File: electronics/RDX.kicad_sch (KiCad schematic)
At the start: 47 parts, among them SW1 Rotary Encoder Module, U1 PCA9685PW

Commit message: revision 1.1.0 of electronics
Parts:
- CTRL.U2: renamed from U1; value PCA9685PW -> PCA9685 - Servo board
- renumbered STEP.J5 to CTRL.J1, CTRL.J1 to CTRL.J2, CTRL.J2 to CTRL.J3, CTRL.J3 to CTRL.J4, PER.M1 to OUT.M1, SW1 to OUT.SW1, PSU.SW2 to OUT.SW2, PER.U1 to OUT.U1
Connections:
- net SDA: now reaches CTRL.J3., CTRL.U1.3 (IO2)
- net SCL: now reaches CTRL.J4., CTRL.U1.5 (IO3)
- new net: STEP.J2., STEP.U2. (B2) (x3)
- new net: STEP.J4., STEP.U4. (B2) (x3)
- new net: STEP.J1., STEP.U1. (B2) (x3)
- new net: STEP.J3., STEP.U3. (B2) (x3)
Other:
- note added: "CTRL.U1.14"
- note added: "PANEL I - Stepper Panel"
- note added: "PANEL II - Control panel"
- note added: "PANEL III - Power panel"
- moved on the sheet: OUT.M1, OUT.STEP1, OUT.STEP2, OUT.STEP3, OUT.STEP4, OUT.SV1, OUT.SV2, OUT.SV3, OUT.SV4, OUT.SV5, OUT.SV6, OUT.SW1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

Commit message: starting electronics and contruction syncronization
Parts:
- renumbered STEP.J1 to A2.J1_1, STEP.J2 to A2.J1_2, STEP.J3 to A2.J1_3, STEP.J4 to A2.J1_4, STEP.U1 to A2.U1_1, STEP.U2 to A2.U1_2, STEP.U3 to A2.U1_3, STEP.U4 to A2.U1_4, PSU.J01 to A4.J01, PSU.J02 to A4.J02, PSU.J11 to A4.J11, PSU.J12 to A4.J12, PSU.J21 to A4.J21, PSU.J22 to A4.J22, PSU.PS1 to A4.PS1, PSU.PS11 to A4.PS11, PSU.PS12 to A4.PS12, PSU.PS13 to A4.PS13
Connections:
- new net: A2.J1_2., A2.U1_2. (B2) (x3)
- new net: A2.J1_4., A2.U1_4. (B2) (x3)
- new net: A2.J1_1., A2.U1_1. (B2) (x3)
- new net: A2.J1_3., A2.U1_3. (B2) (x3)
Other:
- note added: "A2 - PANEL I - Stepper Panel"
- note added: "A3 - PANEL II - Control panel"
- note added: "A3.J2 (5V)"
- note added: "A4 - PANEL III - Power panel"
- note added: "A4.J12 (36V)"
- note added: "The controller includes 4 high performace stepper drivers that can be calibrated for microstepping manually See the table for pin mappings to the RPi GPIOs"
- note removed: "PANEL I - Stepper Panel"
- note removed: "PANEL II - Control panel"
- note removed: "PANEL III - Power panel"
- note removed: "STEP.J5 (5V)"
- note removed: "The controller includes 3 high performace stepper drivers that can be calibrated for microstepping manually See the table for pin mappings to the RPi GPIOs"
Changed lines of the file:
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@@
 		)
 	)
-	(text "PANEL III - Power panel"
+	(text "A4 - PANEL III - Power panel"
 		(exclude_from_sim no)
 		(at 20.32 276.606 0)
@@
 		)
 	)
-	(text "PANEL I - Stepper Panel"
+	(text "A2 - PANEL I - Stepper Panel"
 		(exclude_from_sim no)
 		(at 20.32 21.844 0)
@@
 		)
 	)
-	(text "PANEL II - Control panel"
+	(text "A3 - PANEL II - Control panel"
 		(exclude_from_sim no)
 		(at 299.72 22.352 0)
@@
 		)
 	)
-	(text "The controller includes 3 high performace stepper drivers\nthat can be calibrated for microstepping manually\n\nSee the table for pin mappings to the RPi GPIOs"
+	(text "The controller includes 4 high performace stepper drivers\nthat can be calibrated for microstepping manually\n\nSee the table for pin mappings to the RPi GPIOs"
 		(exclude_from_sim no)
 		(at 121.412 168.91 0)
@@
 		)
 	)
-	(text "PSU.J12 (36V)"
+	(text "A4.J12 (36V)"
 		(exclude_from_sim no)
 		(at 67.818 85.852 0)
@@
 		)
 	)
-	(text "STEP.J5 (5V)"
+	(text "A3.J2 (5V)"
 		(exclude_from_sim no)
 		(at 49.53 85.598 0)
@@
 		)
 	)
+	(polyline
+		(pts
+			(xy 19.05 220.98) (xy 54.61 220.98)
+		)
+		(stroke
+			(width 0)
+			(type dash)
+		)
+	)
 	(wire
 		(pts
@@
 		)
 	)
+	(polyline
+		(pts
+			(xy 54.61 186.69) (xy 54.61 191.77)
+		)
+		(stroke
+			(width 0)
+			(type dash)
+		)
+	)
 	(wire
 		(pts
@@
 		)
 	)
+	(polyline
+		(pts
+			(xy 54.61 201.93) (xy 54.61 220.98)
+		)
+		(stroke
+			(width 0)
+			(type dash)
+		)
+	)
 	(wire
 		(pts
@@
 		(on_board yes)
 		(dnp no)
-		(property "Reference" "PSU.J02"
+		(property "Reference" "A4.J02"
 			(at 99.06 239.776 0)
 			(effects
@@
 			(project "RDX"
 				(path "/ae012dcf-7a16-4b89-bb28-202da592e0ac"
-					(reference "PSU.J02")
+					(reference "A4.J02")
 					(unit 1)
 				)
@@
 		(on_board yes)
 		(dnp no)
-		(property "Reference" "STEP.J2"
+		(property "Reference" "A2.J1_2"
 			(at 106.172 69.85 90)
 			(effects
@@
 			(project "RDX"
 				(path "/ae012dcf-7a16-4b89-bb28-202da592e0ac"
-					(reference "STEP.J2")
+					(reference "A2.J1_2")
 					(unit 1)
 				)
@@
 		(on_board yes)
 		(dnp no)
-		(property "Reference" "STEP.U4"
+		(property "Reference" "A2.U1_4"
 			(at 137.668 109.982 0)
 			(effects
@@
 			(project "RDX"
 				(path "/ae012dcf-7a16-4b89-bb28-202da592e0ac"
-					(reference "STEP.U4")
+					(reference "A2.U1_4")
 					(unit 1)
 				)
@@
 		(on_board yes)
 		(dnp no)
-		(property "Reference" "STEP.J1"
+		(property "Reference" "A2.J1_1"
 			(at 37.592 69.85 90)
 			(effects
@@
 			(project ""
 				(path "/ae012dcf-7a16-4b89-bb28-202da592e0ac"
-					(reference "STEP.J1")
+					(reference "A2.J1_1")
 					(unit 1)
 				)
@@
 		(on_board yes)
 		(dnp no)
-		(property "Reference" "PSU.J22"
+		(property "Reference" "A4.J22"
 			(at 137.16 214.63 0)
 			(effects
@@
 			(project "RDX"
 				(path "/ae012dcf-7a16-4b89-bb28-202da592e0ac"
-					(reference "PSU.J22")
+					(reference "A4.J22")
 					(unit 1)
 				)
@@
 		(on_board yes)
 		(dnp no)
-		(property "Reference" "PSU.J01"
+		(property "Reference" "A4.J01"
 			(at 99.06 229.616 0)
 			(effects
@@
 			(project ""
 				(path "/ae012dcf-7a16-4b89-bb28-202da592e0ac"
-					(reference "PSU.J01")
+					(reference "A4.J01")
 					(unit 1)
 				)
@@
 		(on_board yes)
 		(dnp no)
-		(property "Reference" "STEP.J3"
+		(property "Reference" "A2.J1_3"
 			(at 37.592 142.24 90)
 			(effects
@@
 			(project "RDX"
 				(path "/ae012dcf-7a16-4b89-bb28-202da592e0ac"
-					(reference "STEP.J3")
+					(reference "A2.J1_3")
 					(unit 1)
 				)
@@
 		(dnp no)
 		(fields_autoplaced yes)
-		(property "Reference" "PSU.J21"
+		(property "Reference" "A4.J21"
 			(at 139.7 204.47 0)
 			(effects
@@
 			(project "RDX"
 				(path "/ae012dcf-7a16-4b89-bb28-202da592e0ac"
-					(reference "PSU.J21")
+					(reference "A4.J21")
 					(unit 1)
 				)
@@
 		(on_board yes)
 		(dnp no)
-		(property "Reference" "PSU.PS11"
+		(property "Reference" "A4.PS11"
 			(at 110.49 199.39 0)
 			(effects
@@
 			(project ""
 				(path "/ae012dcf-7a16-4b89-bb28-202da592e0ac"
-					(reference "PSU.PS11")
+					(reference "A4.PS11")
 					(unit 1)
 				)
@@
 		(on_board yes)
 		(dnp no)
-		(property "Reference" "PSU.PS13"
+		(property "Reference" "A4.PS13"
 			(at 125.73 248.92 0)
 			(effects
@@
 			(project "RDX"
 				(path "/ae012dcf-7a16-4b89-bb28-202da592e0ac"
-					(reference "PSU.PS13")
+					(reference "A4.PS13")
 					(unit 1)
 				)
@@
 		(on_board yes)
 		(dnp no)
-		(property "Reference" "STEP.U3"
+		(property "Reference" "A2.U1_3"
 			(at 69.088 109.982 0)
 			(effects
@@
 			(project "RDX"
 				(path "/ae012dcf-7a16-4b89-bb28-202da592e0ac"
-					(reference "STEP.U3")
+					(reference "A2.U1_3")
 					(unit 1)
 				)
@@
 		(on_board yes)
 		(dnp no)
-		(property "Reference" "STEP.J4"
+		(property "Reference" "A2.J1_4"
 			(at 106.172 142.24 90)
 			(effects
@@
 			(project "RDX"
 				(path "/ae012dcf-7a16-4b89-bb28-202da592e0ac"
-					(reference "STEP.J4")
+					(reference "A2.J1_4")
 					(unit 1)
 				)
@@
 		(on_board yes)
 		(dnp no)
-		(property "Reference" "PSU.J12"
+		(property "Reference" "A4.J12"
 			(at 95.504 258.318 90)
 			(effects
@@
 			(project "RDX"
 				(path "/ae012dcf-7a16-4b89-bb28-202da592e0ac"
-					(reference "PSU.J12")
+					(reference "A4.J12")
 					(unit 1)
 				)
@@
 		(on_board yes)
 		(dnp no)
-		(property "Reference" "PSU.PS1"
+		(property "Reference" "A4.PS1"
 			(at 67.31 189.23 0)
 			(effects
@@
 			(project ""
 				(path "/ae012dcf-7a16-4b89-bb28-202da592e0ac"
-					(reference "PSU.PS1")
+					(reference "A4.PS1")
 					(unit 1)
 				)
@@
 		(on_board yes)
 		(dnp no)
-		(property "Reference" "STEP.U2"
+		(property "Reference" "A2.U1_2"
 			(at 137.668 37.592 0)
 			(effects
@@
 			(project "RDX"
 				(path "/ae012dcf-7a16-4b89-bb28-202da592e0ac"
-					(reference "STEP.U2")
+					(reference "A2.U1_2")
 					(unit 1)
 				)
@@
 		(on_board yes)
 		(dnp no)
-		(property "Reference" "STEP.U1"
+		(property "Reference" "A2.U1_1"
 			(at 69.088 37.592 0)
 			(effects
@@
 			(project ""
 				(path "/ae012dcf-7a16-4b89-bb28-202da592e0ac"
-					(reference "STEP.U1")
+					(reference "A2.U1_1")
 					(unit 1)
 				)
@@
 		(on_board yes)
 		(dnp no)
-		(property "Reference" "PSU.J11"
+		(property "Reference" "A4.J11"
 			(at 139.7 186.436 0)
 			(effects
@@
 			(project ""
 				(path "/ae012dcf-7a16-4b89-bb28-202da592e0ac"
-					(reference "PSU.J11")
+					(reference "A4.J11")
 					(unit 1)
 				)
@@
 		(on_board yes)
 		(dnp no)
-		(property "Reference" "PSU.PS12"
+		(property "Reference" "A4.PS12"
 			(at 125.73 227.33 0)
 			(effects
@@
 			(project "RDX"
 				(path "/ae012dcf-7a16-4b89-bb28-202da592e0ac"
-					(reference "PSU.PS12")
+					(reference "A4.PS12")
 					(unit 1)
 				)

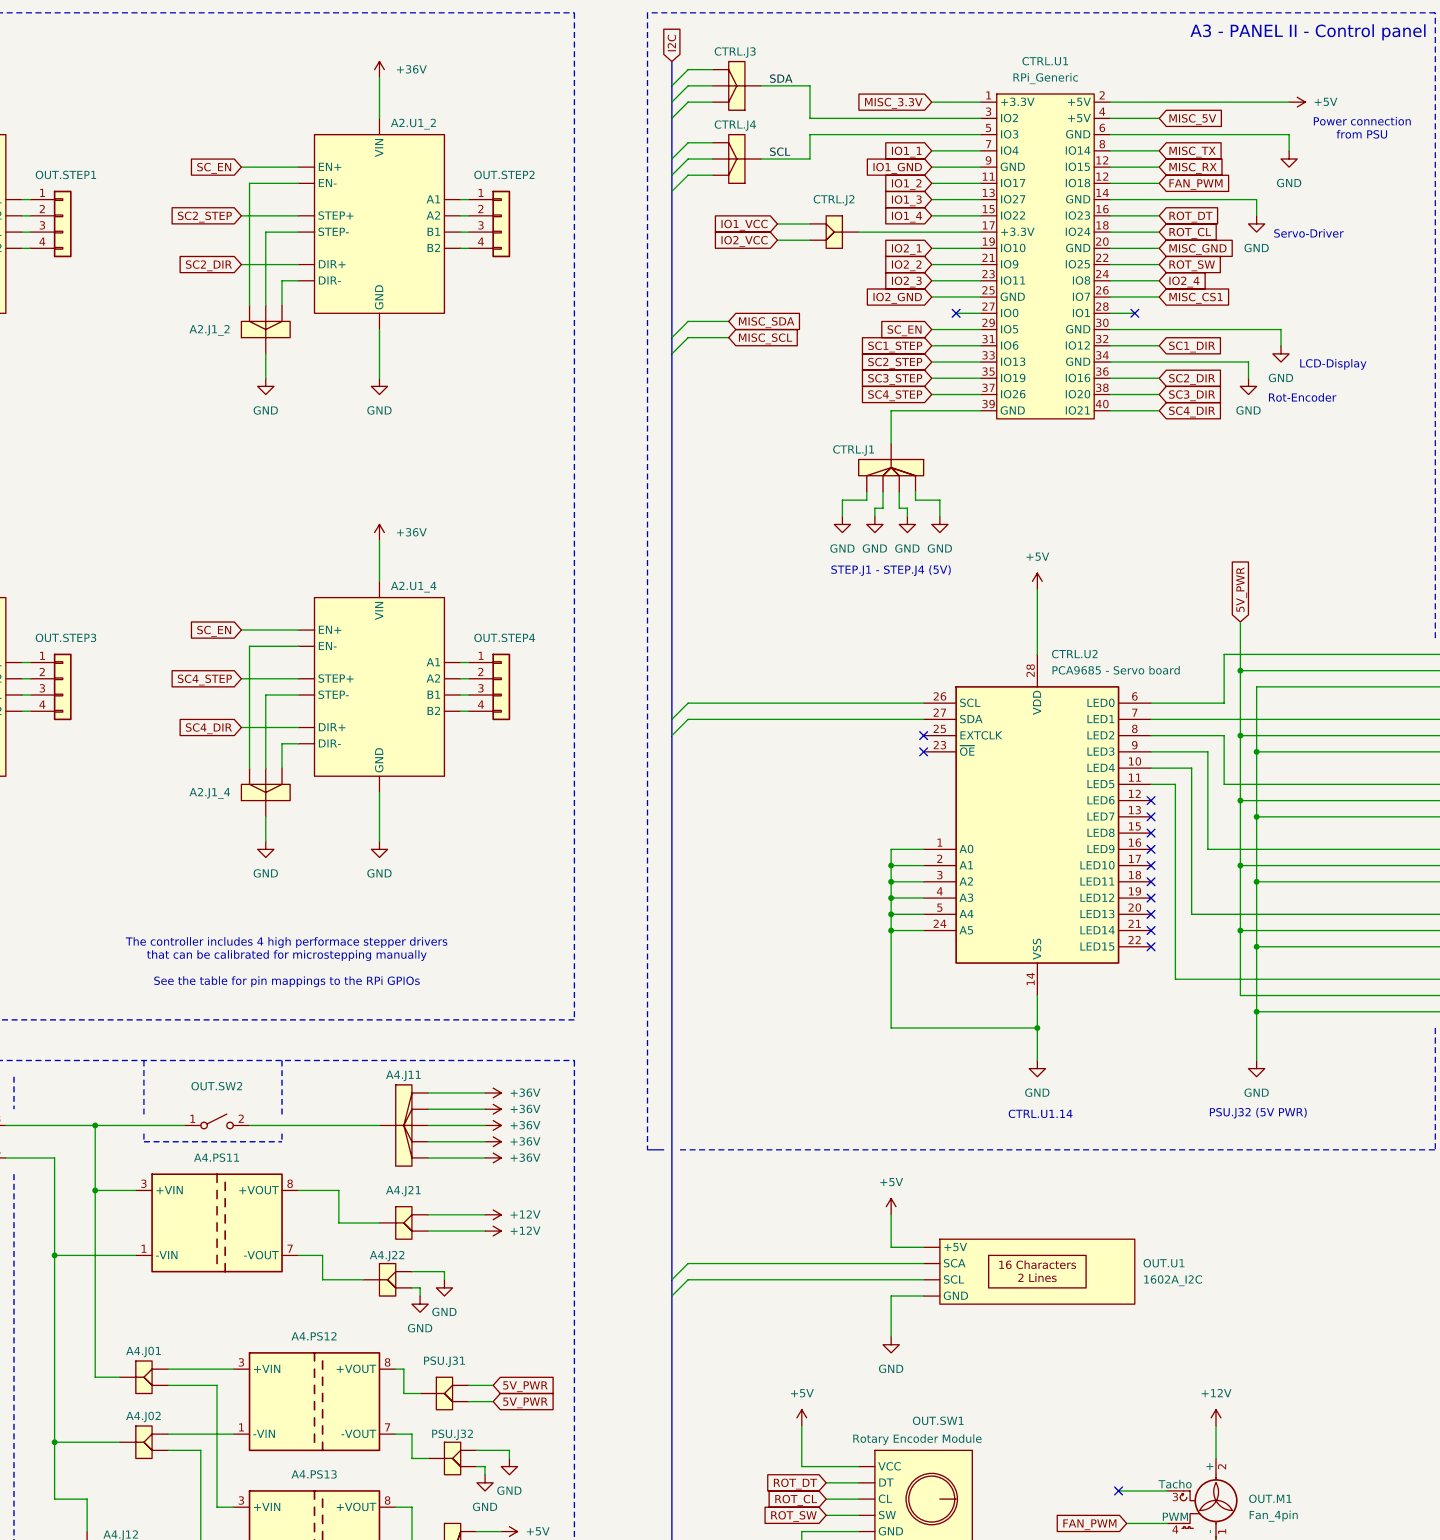
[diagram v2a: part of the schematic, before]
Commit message: further progress on cover parts
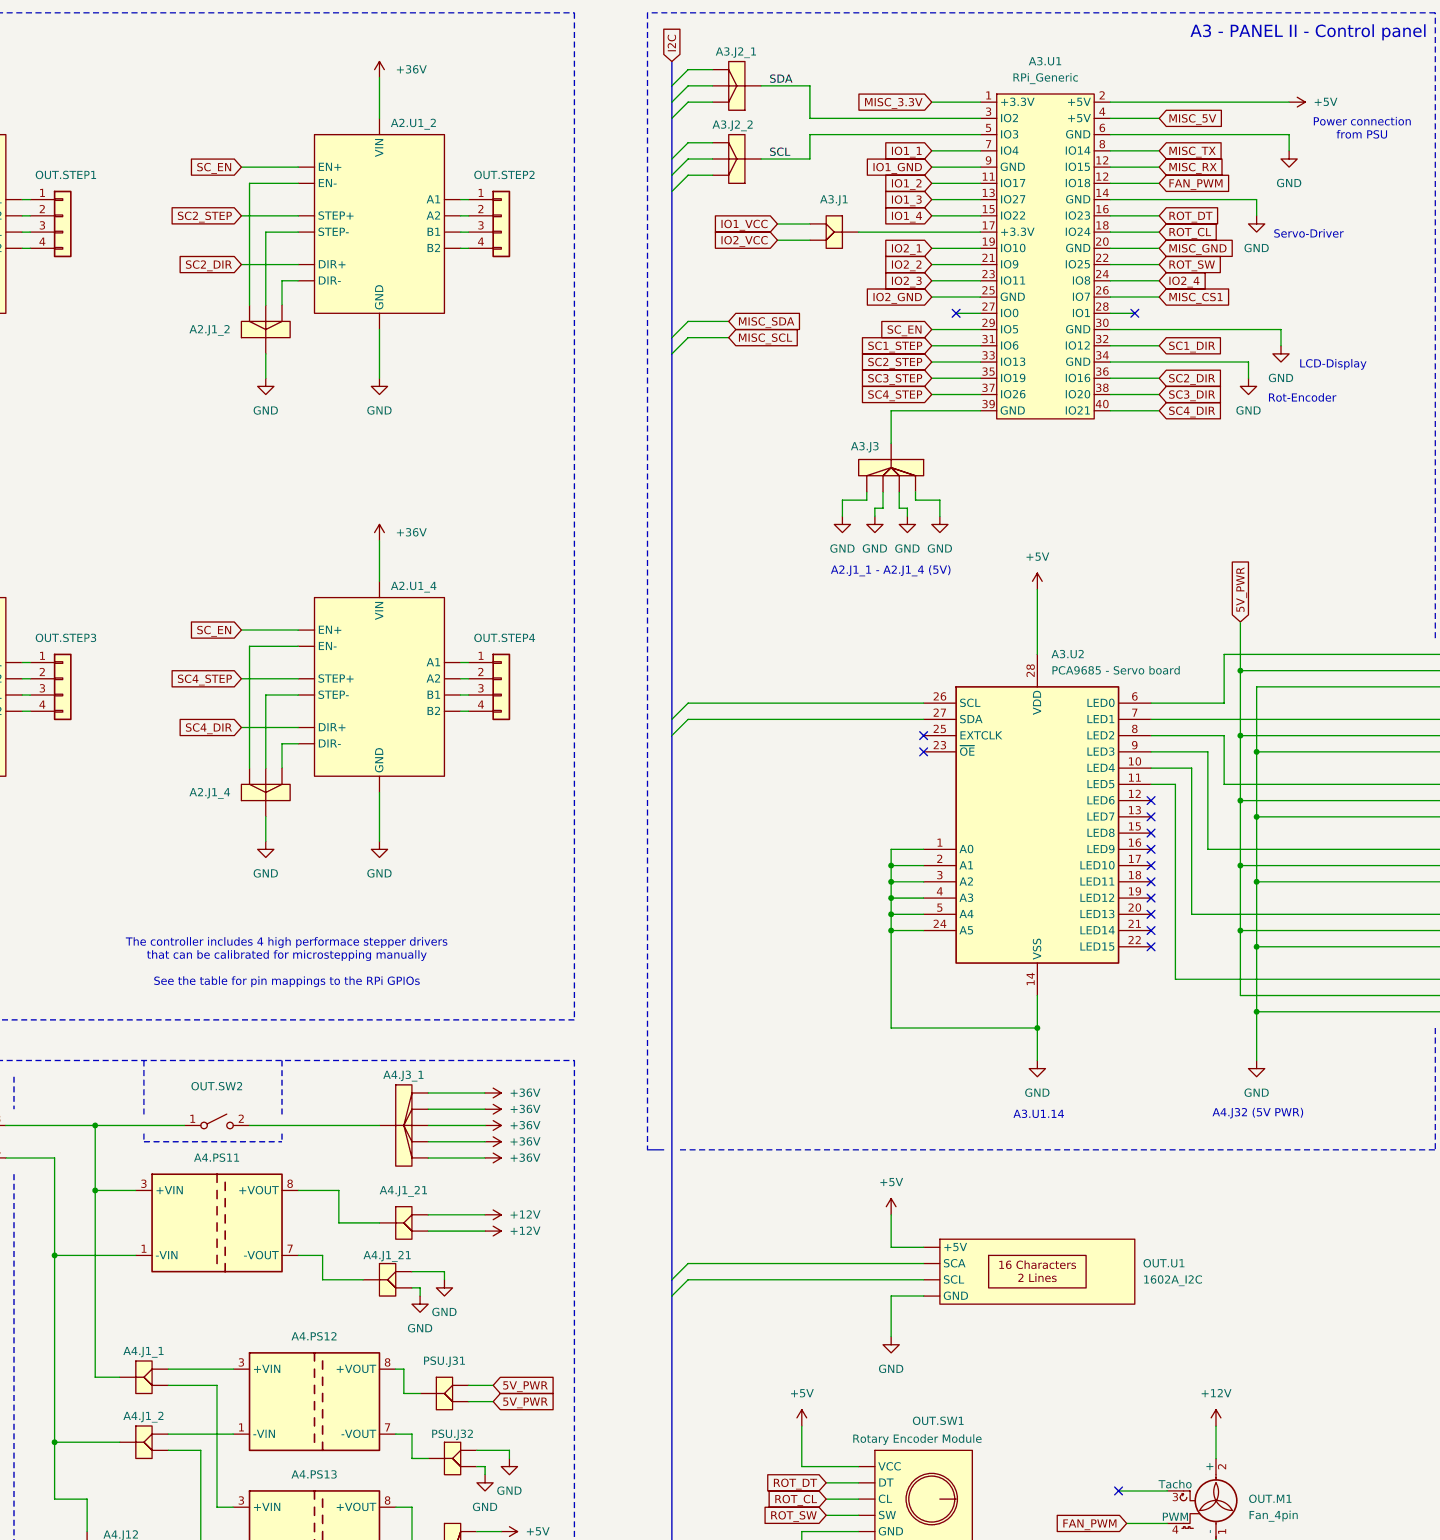
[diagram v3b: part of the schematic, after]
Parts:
- renumbered CTRL.J2 to A3.J1, CTRL.J3 to A3.J2_1, CTRL.J4 to A3.J2_2, CTRL.J1 to A3.J3, CTRL.U1 to A3.U1, CTRL.U2 to A3.U2, A4.J01 to A4.J1_1, A4.J02 to A4.J1_2, A4.J22 to A4.J1_21, A4.J21 to A4.J1_21, A4.J11 to A4.J3_1
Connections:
- new net: A2.J1_2., A2.U1_2. (B2) (x3)
- new net: A2.J1_4., A2.U1_4. (B2) (x3)
- new net: A2.J1_1., A2.U1_1. (B2) (x3)
- new net: A2.J1_3., A2.U1_3. (B2) (x3)
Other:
- note added: "A2.J1_1 - A2.J1_4 (5V)"
- note added: "A3.U1.14"
- note added: "A4.J32 (5V PWR)"
- note removed: "CTRL.U1.14"
- note removed: "PSU.J32 (5V PWR)"
- note removed: "STEP.J1 - STEP.J4 (5V)"
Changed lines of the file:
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@@
 		)
 	)
-	(text "CTRL.U1.14"
+	(text "A3.U1.14"
 		(exclude_from_sim no)
-		(at 239.268 192.786 0)
+		(at 239.014 192.786 0)
 		(effects
 			(font
@@
 		)
 	)
-	(text "PSU.J32 (5V PWR)"
+	(text "A4.J32 (5V PWR)"
 		(exclude_from_sim no)
 		(at 273.304 192.532 0)
@@
 		)
 	)
-	(text "STEP.J1 - STEP.J4 (5V)"
+	(text "A2.J1_1 - A2.J1_4 (5V)"
 		(exclude_from_sim no)
 		(at 215.9 107.696 0)
@@
 		(on_board yes)
 		(dnp no)
-		(property "Reference" "A4.J02"
+		(property "Reference" "A4.J1_2"
 			(at 99.06 239.776 0)
 			(effects
@@
 			(project "RDX"
 				(path "/ae012dcf-7a16-4b89-bb28-202da592e0ac"
-					(reference "A4.J02")
+					(reference "A4.J1_2")
 					(unit 1)
 				)
@@
 		(on_board yes)
 		(dnp no)
-		(property "Reference" "CTRL.J1"
-			(at 210.058 88.646 90)
+		(property "Reference" "A3.J3"
+			(at 211.836 88.138 90)
 			(effects
 				(font
@@
 			(project "RDX"
 				(path "/ae012dcf-7a16-4b89-bb28-202da592e0ac"
-					(reference "CTRL.J1")
+					(reference "A3.J3")
 					(unit 1)
 				)
@@
 		(dnp no)
 		(fields_autoplaced yes)
-		(property "Reference" "CTRL.U2"
+		(property "Reference" "A3.U2"
 			(at 240.9541 120.65 0)
 			(effects
@@
 			(project ""
 				(path "/ae012dcf-7a16-4b89-bb28-202da592e0ac"
-					(reference "CTRL.U2")
+					(reference "A3.U2")
 					(unit 1)
 				)
@@
 		(on_board yes)
 		(dnp no)
-		(property "Reference" "A4.J22"
+		(property "Reference" "A4.J1_21"
 			(at 137.16 214.63 0)
 			(effects
@@
 			(project "RDX"
 				(path "/ae012dcf-7a16-4b89-bb28-202da592e0ac"
-					(reference "A4.J22")
+					(reference "A4.J1_21")
 					(unit 1)
 				)
@@
 		(dnp no)
 		(fields_autoplaced yes)
-		(property "Reference" "CTRL.J2"
+		(property "Reference" "A3.J1"
 			(at 207.01 49.53 0)
 			(effects
@@
 			(project ""
 				(path "/ae012dcf-7a16-4b89-bb28-202da592e0ac"
-					(reference "CTRL.J2")
+					(reference "A3.J1")
 					(unit 1)
 				)
@@
 		(on_board yes)
 		(dnp no)
-		(property "Reference" "CTRL.U1"
+		(property "Reference" "A3.U1"
 			(at 240.03 27.94 0)
 			(effects
@@
 			(project ""
 				(path "/ae012dcf-7a16-4b89-bb28-202da592e0ac"
-					(reference "CTRL.U1")
+					(reference "A3.U1")
 					(unit 1)
 				)
@@
 		(on_board yes)
 		(dnp no)
-		(property "Reference" "A4.J01"
+		(property "Reference" "A4.J1_1"
 			(at 99.06 229.616 0)
 			(effects
@@
 			(project ""
 				(path "/ae012dcf-7a16-4b89-bb28-202da592e0ac"
-					(reference "A4.J01")
+					(reference "A4.J1_1")
 					(unit 1)
 				)
@@
 		(on_board yes)
 		(dnp no)
-		(property "Reference" "CTRL.J3"
-			(at 188.214 26.416 0)
+		(property "Reference" "A3.J2_1"
+			(at 188.468 26.416 0)
 			(effects
 				(font
@@
 			(project "RDX"
 				(path "/ae012dcf-7a16-4b89-bb28-202da592e0ac"
-					(reference "CTRL.J3")
+					(reference "A3.J2_1")
 					(unit 1)
 				)
@@
 		(on_board yes)
 		(dnp no)
-		(property "Reference" "CTRL.J4"
-			(at 188.214 37.846 0)
+		(property "Reference" "A3.J2_2"
+			(at 187.96 37.846 0)
 			(effects
 				(font
@@
 			(project "RDX"
 				(path "/ae012dcf-7a16-4b89-bb28-202da592e0ac"
-					(reference "CTRL.J4")
+					(reference "A3.J2_2")
 					(unit 1)
 				)
@@
 		(dnp no)
 		(fields_autoplaced yes)
-		(property "Reference" "A4.J21"
+		(property "Reference" "A4.J1_21"
 			(at 139.7 204.47 0)
 			(effects
@@
 			(project "RDX"
 				(path "/ae012dcf-7a16-4b89-bb28-202da592e0ac"
-					(reference "A4.J21")
+					(reference "A4.J1_21")
 					(unit 1)
 				)
@@
 		(on_board yes)
 		(dnp no)
-		(property "Reference" "A4.J11"
+		(property "Reference" "A4.J3_1"
 			(at 139.7 186.436 0)
 			(effects
@@
 			(project ""
 				(path "/ae012dcf-7a16-4b89-bb28-202da592e0ac"
-					(reference "A4.J11")
+					(reference "A4.J3_1")
 					(unit 1)
 				)
